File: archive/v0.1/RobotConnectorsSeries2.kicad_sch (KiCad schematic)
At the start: 15 parts, among them U6 LM339

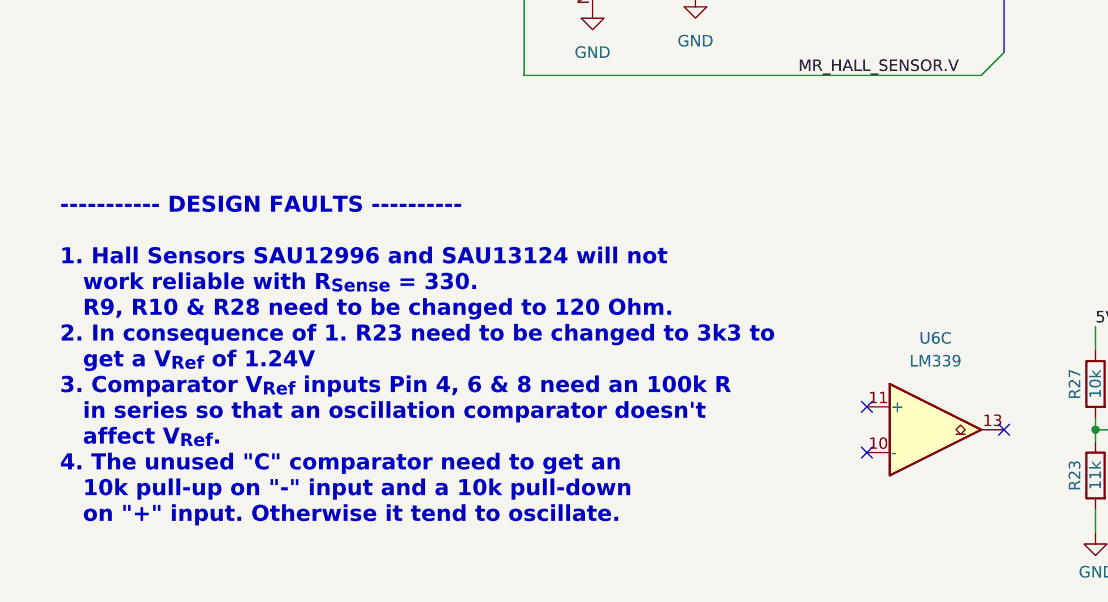
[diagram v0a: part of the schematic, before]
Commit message: Recent v0.1 and CoverUI discoveries
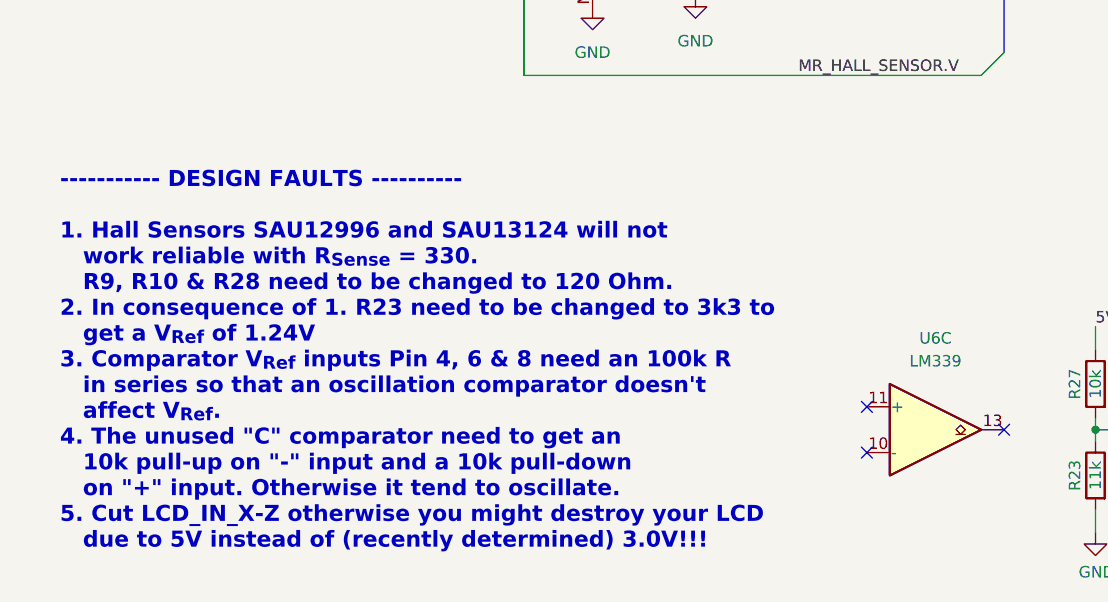
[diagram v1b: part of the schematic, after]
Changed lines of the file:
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@@
 		)
 	)
-	(text "----------- DESIGN FAULTS ----------\n\n1. Hall Sensors SAU12996 and SAU13124 will not\n   work reliable with R_{Sense} = 330.\n   R9, R10 & R28 need to be changed to 120 Ohm.\n2. In consequence of 1. R23 need to be changed to 3k3 to\n   get a V_{Ref} of 1.24V\n3. Comparator V_{Ref} inputs Pin 4, 6 & 8 need an 100k R\n   in series so that an oscillation comparator doesn't\n   affect V_{Ref}.\n4. The unused \"C\" comparator need to get an\n   10k pull-up on \"-\" input and a 10k pull-down\n   on \"+\" input. Otherwise it tend to oscillate."
+	(text "----------- DESIGN FAULTS ----------\n\n1. Hall Sensors SAU12996 and SAU13124 will not\n   work reliable with R_{Sense} = 330.\n   R9, R10 & R28 need to be changed to 120 Ohm.\n2. In consequence of 1. R23 need to be changed to 3k3 to\n   get a V_{Ref} of 1.24V\n3. Comparator V_{Ref} inputs Pin 4, 6 & 8 need an 100k R\n   in series so that an oscillation comparator doesn't\n   affect V_{Ref}.\n4. The unused \"C\" comparator need to get an\n   10k pull-up on \"-\" input and a 10k pull-down\n   on \"+\" input. Otherwise it tend to oscillate.\n5. Cut LCD_IN_X-Z otherwise you might destroy your LCD\n   due to 5V instead of (recently determined) 3.0V!!!"
 		(exclude_from_sim no)
 		(at 19.558 170.18 0)
